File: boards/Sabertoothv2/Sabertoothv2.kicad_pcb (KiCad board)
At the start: 2 copper layers, 41.3 x 41.3 mm, 40 parts, among them J1 Screw_Terminal_01x04, J2 Screw_Terminal_01x04, J4 Conn_01x04_Pin, J5 Conn_01x04_Pin, Q1 NMOS, Q2 NMOS, Q3 NMOS, Q4 NMOS, U1 LM2104, U2 LM2104, U4 74LVC1GU04DRL

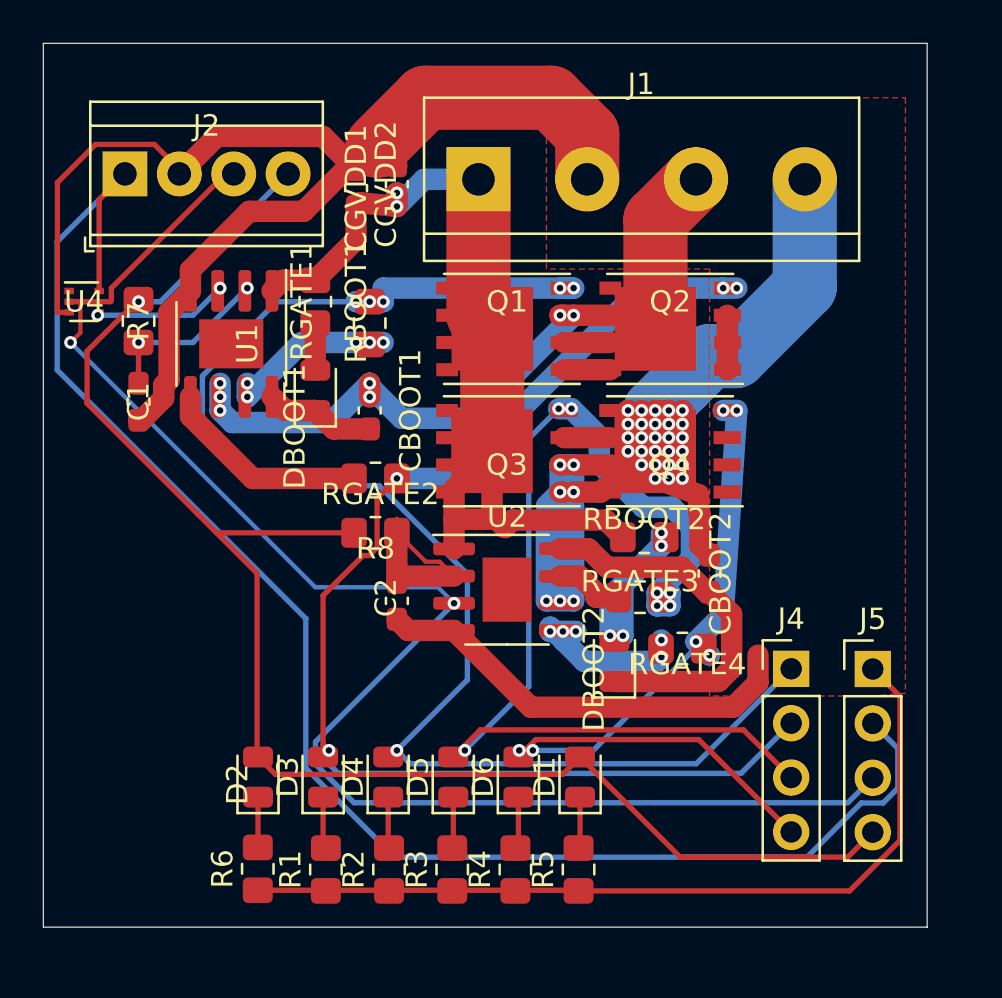
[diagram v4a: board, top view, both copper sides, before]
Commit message: silkscreen update again
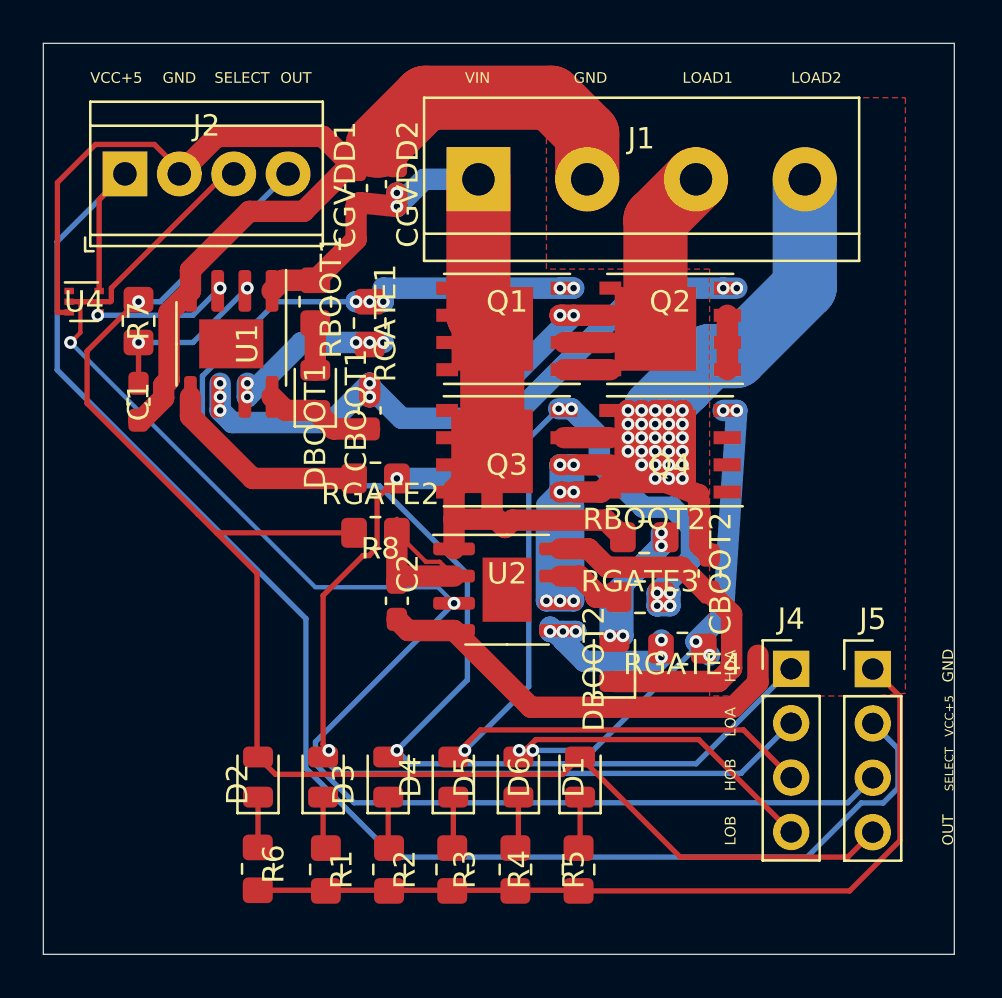
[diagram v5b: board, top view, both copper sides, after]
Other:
- board size 41.3 x 41.3 mm -> 42.5 x 42.5 mm
- board text added: "GND"
- board text added: "HOA"
- board text added: "HOB"
- board text added: "LOA"
- board text added: "LOAD1"
- board text added: "LOAD2"
- board text added: "LOB"
- board text added: "OUT"
- board text added: "SELECT"
- board text added: "VCC+5"
- board text added: "VIN"
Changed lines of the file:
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@@
     (property "ki_keywords" "cap capacitor")
     (attr smd)
-    (fp_text reference "CGVDD2" (at 0 -0.51 90) (layer "F.SilkS")
+    (fp_text reference "CGVDD2" (at 0 0.51 90) (layer "F.SilkS")
         (effects (font (size 1 1) (thickness 0.15)))
     )
@@
     (property "ki_keywords" "cap capacitor")
     (attr smd)
-    (fp_text reference "CBOOT1" (at 0 1.905 90) (layer "F.SilkS")
+    (fp_text reference "CBOOT1" (at 0 -0.635 90) (layer "F.SilkS")
         (effects (font (size 1 1) (thickness 0.15)))
     )
@@
     (property "ki_keywords" "LED diode")
     (attr smd)
-    (fp_text reference "D1" (at 0 -1.65 90) (layer "F.SilkS")
+    (fp_text reference "D1" (at 0 -0.3 90) (layer "F.SilkS")
         (effects (font (size 1 1) (thickness 0.15)))
     )
@@
     (property "ki_keywords" "LED diode")
     (attr smd)
-    (fp_text reference "D5" (at 0 -1.65 90) (layer "F.SilkS")
+    (fp_text reference "D5" (at 0 0.54 90) (layer "F.SilkS")
         (effects (font (size 1 1) (thickness 0.15)))
     )
@@
     (property "ki_keywords" "R res resistor")
     (attr smd)
-    (fp_text reference "RGATE1" (at 1 -3.175 90) (layer "F.SilkS")
+    (fp_text reference "RGATE1" (at 0 0.735 90) (layer "F.SilkS")
         (effects (font (size 1 1) (thickness 0.15)))
     )
@@
     (property "ki_keywords" "R res resistor")
     (attr smd)
-    (fp_text reference "R2" (at 0 -1.65 90) (layer "F.SilkS")
+    (fp_text reference "R2" (at 0 0.735 90) (layer "F.SilkS")
         (effects (font (size 1 1) (thickness 0.15)))
     )
@@
     (property "ki_keywords" "R res resistor")
     (attr smd)
-    (fp_text reference "R1" (at 0 -1.65 90) (layer "F.SilkS")
+    (fp_text reference "R1" (at 0 0.735 90) (layer "F.SilkS")
         (effects (font (size 1 1) (thickness 0.15)))
     )
@@
     (property "ki_keywords" "LED diode")
     (attr smd)
-    (fp_text reference "D4" (at 0 -1.65 90) (layer "F.SilkS")
+    (fp_text reference "D4" (at 0 1.04 90) (layer "F.SilkS")
         (effects (font (size 1 1) (thickness 0.15)))
     )
@@
     (property "ki_keywords" "screw terminal")
     (attr through_hole)
-    (fp_text reference "J1" (at 7.6 -4.445) (layer "F.SilkS")
+    (fp_text reference "J1" (at 7.6 -1.905) (layer "F.SilkS")
         (effects (font (size 1 1) (thickness 0.15)))
     )
@@
     (property "ki_keywords" "R res resistor")
     (attr smd)
-    (fp_text reference "RBOOT1" (at 0 -1.905 90) (layer "F.SilkS")
+    (fp_text reference "RBOOT1" (at -0.227064 -0.735 90) (layer "F.SilkS")
         (effects (font (size 1 1) (thickness 0.15)))
     )
@@
     (property "ki_keywords" "cap capacitor")
     (attr smd)
-    (fp_text reference "C2" (at -0.146267 0.51 90) (layer "F.SilkS")
+    (fp_text reference "C2" (at -1.27 -0.51 90) (layer "F.SilkS")
         (effects (font (size 1 1) (thickness 0.15)))
     )
@@
     (property "ki_keywords" "R res resistor")
     (attr smd)
-    (fp_text reference "R4" (at 0 -1.65 90) (layer "F.SilkS")
+    (fp_text reference "R4" (at 0 0.18 90) (layer "F.SilkS")
         (effects (font (size 1 1) (thickness 0.15)))
     )
@@
     (property "ki_keywords" "cap capacitor")
     (attr smd)
-    (fp_text reference "CGVDD1" (at 0 0 90) (layer "F.SilkS")
+    (fp_text reference "CGVDD1" (at 0.146267 -0.51 90) (layer "F.SilkS")
         (effects (font (size 1 1) (thickness 0.15)))
     )
@@
     (property "ki_keywords" "driver rs485 rs422 differential")
     (attr smd)
-    (fp_text reference "U2" (at 0 -3.4) (layer "F.SilkS")
+    (fp_text reference "U2" (at 0 -0.75) (layer "F.SilkS")
         (effects (font (size 1 1) (thickness 0.15)))
     )
@@
     (property "ki_keywords" "LED diode")
     (attr smd)
-    (fp_text reference "D3" (at 0 -1.65 90) (layer "F.SilkS")
+    (fp_text reference "D3" (at -0.3425 0.96 90) (layer "F.SilkS")
         (effects (font (size 1 1) (thickness 0.15)))
     )
@@
     (property "ki_keywords" "R res resistor")
     (attr smd)
-    (fp_text reference "R6" (at 0 -1.65 90) (layer "F.SilkS")
+    (fp_text reference "R6" (at 0.227064 0.735 90) (layer "F.SilkS")
         (effects (font (size 1 1) (thickness 0.15)))
     )
@@
     (property "ki_keywords" "LED diode")
     (attr smd)
-    (fp_text reference "D6" (at 0 -1.65 90) (layer "F.SilkS")
+    (fp_text reference "D6" (at 0 0.04 90) (layer "F.SilkS")
         (effects (font (size 1 1) (thickness 0.15)))
     )
@@
     (property "ki_keywords" "R res resistor")
     (attr smd)
-    (fp_text reference "RGATE4" (at 0.227064 0.735) (layer "F.SilkS")
+    (fp_text reference "RGATE4" (at 0 0.735) (layer "F.SilkS")
         (effects (font (size 1 1) (thickness 0.15)))
     )
@@
     (property "ki_keywords" "diode")
     (attr smd)
-    (fp_text reference "DBOOT1" (at -1.685 -0.96 90) (layer "F.SilkS")
+    (fp_text reference "DBOOT1" (at -1.685 0 90) (layer "F.SilkS")
         (effects (font (size 1 1) (thickness 0.15)))
     )
@@
     (property "ki_keywords" "R res resistor")
     (attr smd)
-    (fp_text reference "R3" (at 0 -1.65 90) (layer "F.SilkS")
+    (fp_text reference "R3" (at 0 0.59 90) (layer "F.SilkS")
         (effects (font (size 1 1) (thickness 0.15)))
     )
@@
     (property "ki_keywords" "R res resistor")
     (attr smd)
-    (fp_text reference "R8" (at 0 0.735) (layer "F.SilkS")
+    (fp_text reference "R8" (at 0.227064 0.735) (layer "F.SilkS")
         (effects (font (size 1 1) (thickness 0.15)))
     )
@@
     (property "ki_keywords" "R res resistor")
     (attr smd)
-    (fp_text reference "R5" (at 0 -1.65 90) (layer "F.SilkS")
+    (fp_text reference "R5" (at 0 -0.23 90) (layer "F.SilkS")
         (effects (font (size 1 1) (thickness 0.15)))
     )
@@
   (gr_rect (start 63.5 47.625) (end 78.74 57.785)
     (stroke (width 0.1) (type default)) (fill none) (layer "B.SilkS"))
-  (gr_rect (start 51.435 20.32) (end 92.71 61.595)
+  (gr_rect (start 51.435 20.32) (end 93.98 62.865)
     (stroke (width 0.05) (type default)) (fill none) (layer "Edge.Cuts"))
   (gr_text "Nathan Colunga\nLee Buffett\nEmily Lory\nJoseph Hanger" (at 71.12 55.245) (layer "B.SilkS")
     (effects (font (size 1 1) (thickness 0.15)) (justify bottom mirror))
   )
+  (gr_text "LOAD1" (at 81.28 22.225) (layer "F.SilkS")
+    (effects (font (size 0.5 0.5) (thickness 0.1)) (justify left bottom))
+  )
+  (gr_text "VCC+5" (at 53.625 22.225) (layer "F.SilkS")
+    (effects (font (size 0.5 0.5) (thickness 0.1)) (justify left bottom))
+  )
+  (gr_text "GND" (at 93.98 50.165 90) (layer "F.SilkS")
+    (effects (font (size 0.5 0.5) (thickness 0.1)) (justify left bottom))
+  )
+  (gr_text "VIN\n" (at 71.12 22.225) (layer "F.SilkS")
+    (effects (font (size 0.5 0.5) (thickness 0.1)) (justify left bottom))
+  )
+  (gr_text "SELECT" (at 59.42 22.225) (layer "F.SilkS")
+    (effects (font (size 0.5 0.5) (thickness 0.1)) (justify left bottom))
+  )
+  (gr_text "LOAD2" (at 86.36 22.225) (layer "F.SilkS")
+    (effects (font (size 0.5 0.5) (thickness 0.1)) (justify left bottom))
+  )
+  (gr_text "SELECT" (at 93.98 55.245 90) (layer "F.SilkS")
+    (effects (font (size 0.4 0.4) (thickness 0.1)) (justify left bottom))
+  )
+  (gr_text "HOA" (at 83.82 50.165 90) (layer "F.SilkS")
+    (effects (font (size 0.5 0.5) (thickness 0.1)) (justify left bottom))
+  )
+  (gr_text "HOB" (at 83.82 55.245 90) (layer "F.SilkS")
+    (effects (font (size 0.5 0.5) (thickness 0.1)) (justify left bottom))
+  )
+  (gr_text "LOB" (at 83.82 57.785 90) (layer "F.SilkS")
+    (effects (font (size 0.5 0.5) (thickness 0.1)) (justify left bottom))
+  )
+  (gr_text "OUT\n" (at 62.5 22.225) (layer "F.SilkS")
+    (effects (font (size 0.5 0.5) (thickness 0.1)) (justify left bottom))
+  )
+  (gr_text "VCC+5" (at 93.98 52.705 90) (layer "F.SilkS")
+    (effects (font (size 0.4 0.4) (thickness 0.1)) (justify left bottom))
+  )
+  (gr_text "GND" (at 57 22.225) (layer "F.SilkS")
+    (effects (font (size 0.5 0.5) (thickness 0.1)) (justify left bottom))
+  )
+  (gr_text "OUT" (at 93.98 57.785 90) (layer "F.SilkS")
+    (effects (font (size 0.5 0.5) (thickness 0.1)) (justify left bottom))
+  )
+  (gr_text "GND" (at 76.2 22.225) (layer "F.SilkS")
+    (effects (font (size 0.5 0.5) (thickness 0.1)) (justify left bottom))
+  )
+  (gr_text "LOA" (at 83.82 52.705 90) (layer "F.SilkS")
+    (effects (font (size 0.5 0.5) (thickness 0.1)) (justify left bottom))
+  )
   (segment (start 55.88 36.195) (end 55.88 34.29) (width 0.25) (layer "F.Cu") (net 1))

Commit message: got rid of most warnings on DRC
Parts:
- moved DBOOT 0.94 mm to (64.1, 37.5)
- moved CBOOT 0.53 mm to (66.1, 37.5)
- renumbered CBOOT2 to CBOOT, CBOOT1 to CBOOT, CGVDD2 to CGVD, CGVDD1 to CGVD, DBOOT2 to DBOOT, DBOOT1 to DBOOT, RBOOT1 to RBOOT, RBOOT2 to RBOOT, RGATE1 to RGATE, RGATE3 to RGATE, RGATE2 to RGATE, RGATE4 to RGATE

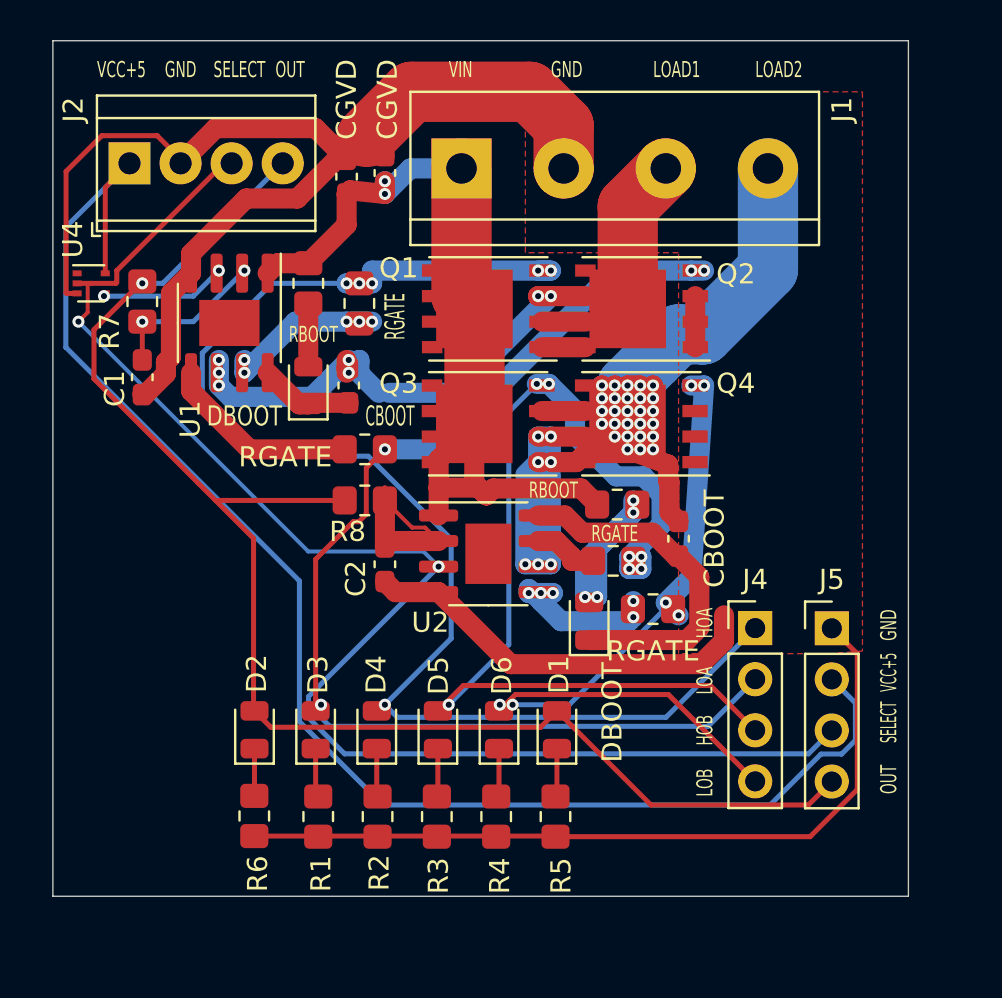
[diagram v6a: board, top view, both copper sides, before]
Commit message: fixed via positions and readjusted traces
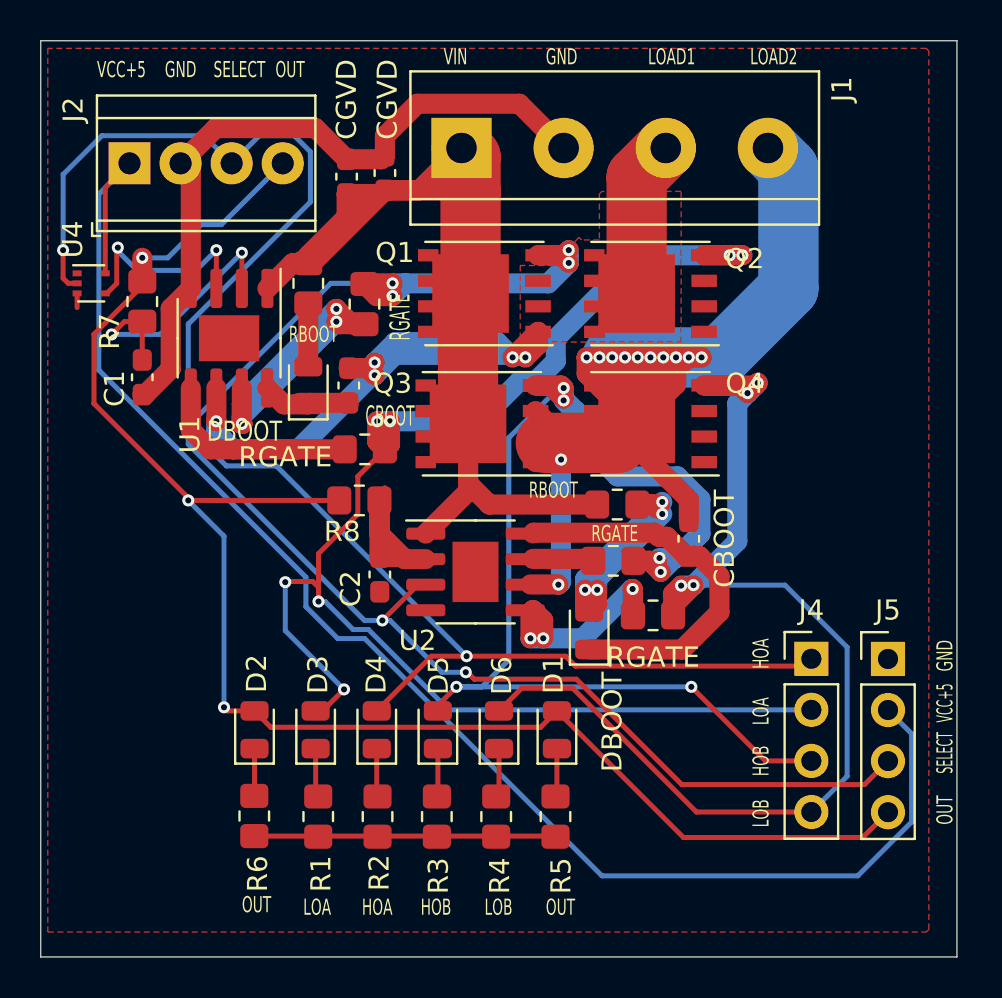
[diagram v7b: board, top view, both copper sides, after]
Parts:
- moved J4 3.18 mm to (89.2, 51.1)
- moved J5 3.18 mm to (93.0, 51.1)
- moved U2 1.10 mm to (72.5, 46.7)
- moved J1 1.02 mm to (71.8, 25.7)
- moved Q2 0.88 mm to (81.2, 32.9)
- moved Q1 0.79 mm to (72.9, 32.9)
- moved U1 0.76 mm to (60.2, 35.1)
- moved C2 0.57 mm to (67.7, 46.9)
- moved CBOOT 0.51 mm to (83.1, 45.1)
- moved DBOOT 0.47 mm to (78.1, 49.7)
- moved Q4 0.45 mm to (81.2, 39.4)
- moved RGATE 0.31 mm to (81.3, 48.9)
- moved Q3 0.31 mm to (72.8, 39.4)
- moved R8 0.27 mm to (66.7, 43.2)
- moved RGATE 0.26 mm to (66.9, 33.4)
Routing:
- net GND: track 119.9 -> 51.5 mm
- net LOB: track 38.3 -> 57.0 mm, vias 6 -> 4
- net LOAD2: track 78.1 -> 95.3 mm, vias 34 -> 12
- net LOA: track 57.8 -> 73.3 mm, vias 4 -> 7
- net Net-(U1-GH): track 8.04 -> 19.7 mm, vias 5 -> 3
- net HOB: track 50.9 -> 61.5 mm, vias 7 -> 6
- net SELECT: track 73.2 -> 82.9 mm, vias 2 -> 3
- net VIN: track 44.5 -> 51.1 mm, vias 2 -> 0
- net Net-(U1-IN): track 8.04 -> 13.8 mm
- net LOAD1: track 37.4 -> 42.7 mm, vias 7 -> 5
- net OUT: track 74.6 -> 79.6 mm, vias 1 -> 3
- net Net-(DBOOT2-A): track 11.3 -> 15.7 mm
- net Net-(U1-SD'): track 6.24 -> 10.4 mm
- net HOA: track 68.1 -> 71.5 mm, vias 6 -> 5
- net Net-(U2-GL): track 8.58 -> 10.5 mm, vias 5 -> 3
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- added copper zone on F.Cu, net LOAD1
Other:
- board size 42.5 x 42.5 mm -> 45.6 x 45.6 mm
- board text added: "JLCJLCJLCJLC"
